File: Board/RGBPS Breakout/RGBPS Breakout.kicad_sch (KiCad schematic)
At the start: 2 parts, among them IC1 APDS-9999, J1 Conn_01x04_Pin

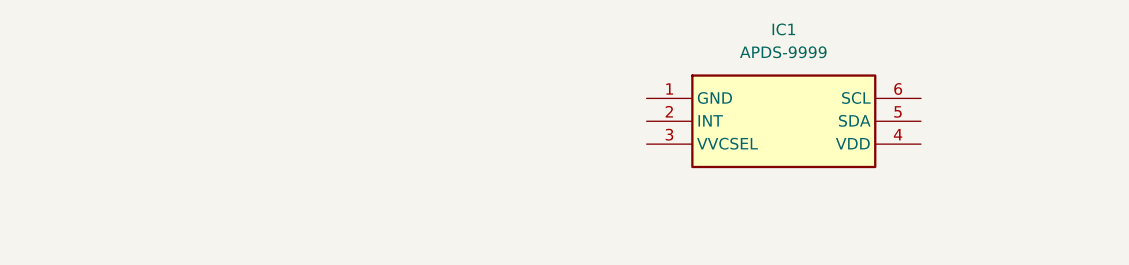
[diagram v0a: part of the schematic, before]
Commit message: indicator/illuminating LED
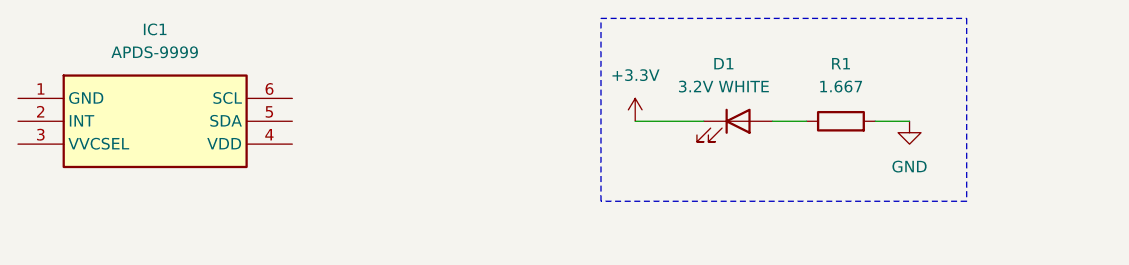
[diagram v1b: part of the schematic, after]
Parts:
- added D1: 3.2V WHITE, symbol Device:LED
- added R1: 1.667, symbol Device:R
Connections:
- net +3.3V: now also D1.1 (K)
- net GND: now also R1.2
- new net: D1.2 (A), R1.1
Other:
- moved on the sheet: IC1

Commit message: partially done with power
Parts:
- added C1, C2: 4u7, symbol Device:C
- added R2: 100, symbol Device:R
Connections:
- net +3.3V: now also IC1.3 (VVCSEL), C2.1, R2.2
- net GND: now also IC1.1 (GND), C1.2, C2.2
- net at IC1.4 (VDD): now also C1.1, R2.1
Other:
- moved on the sheet: D1, IC1, J1, R1

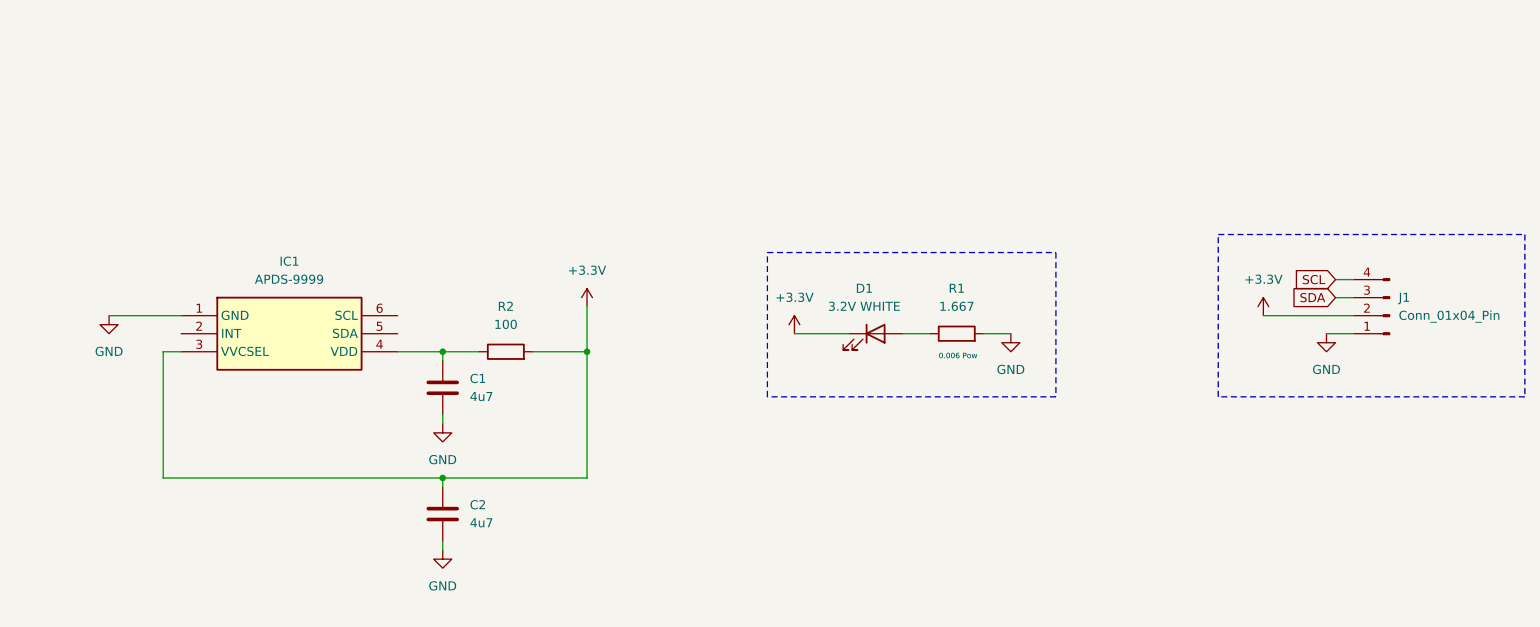
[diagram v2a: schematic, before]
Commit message: i2c wiring + pullup resistors
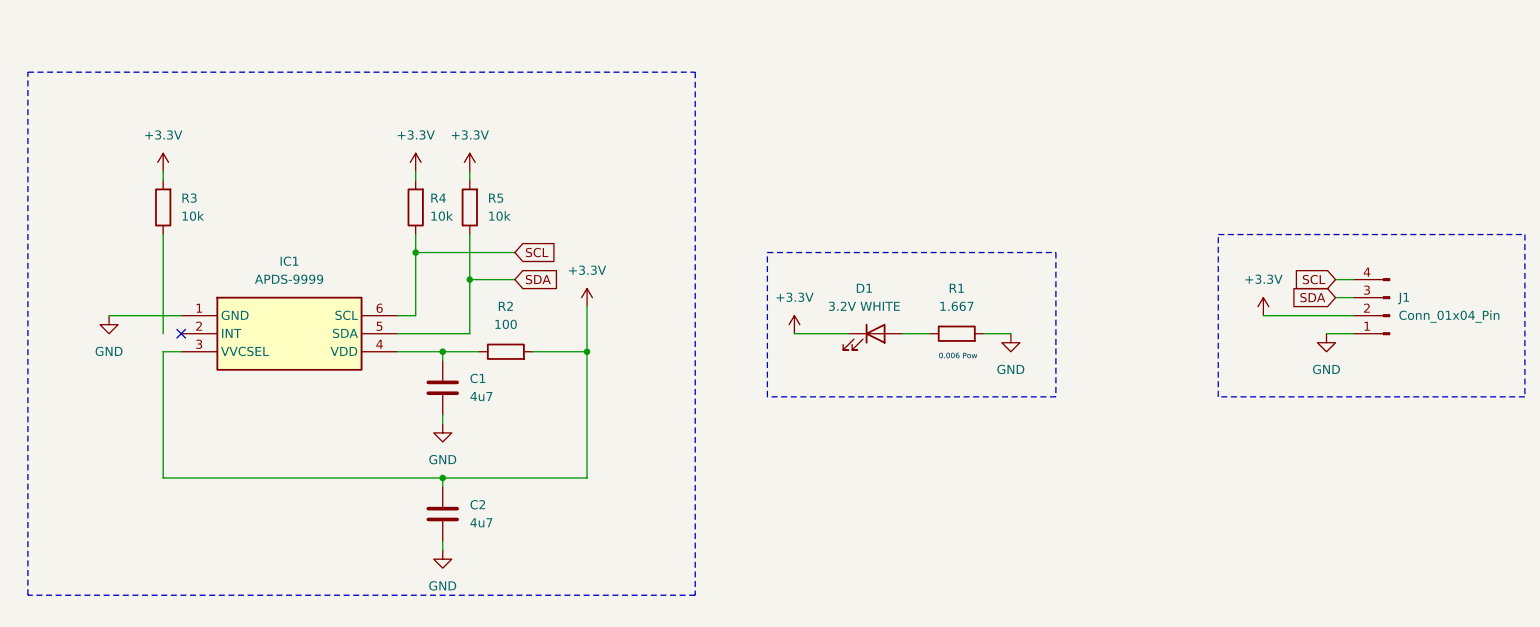
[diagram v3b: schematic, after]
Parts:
- added R3, R4, R5: 10k, symbol Device:R
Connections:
- net +3.3V: now also R3.2, R4.2, R5.2
- net SCL: now also IC1.6 (SCL), R4.1
- net SDA: now also IC1.5 (SDA), R5.1
- no-connect marks 0 -> 1

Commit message: interrupt pin
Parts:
- added J2: Conn_01x01_Pin, symbol Connector:Conn_01x01_Pin
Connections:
- net INT: now reaches IC1.2 (INT)
- net INT: now also R3.1, J2.1 (Pin_1)
- no-connect marks 1 -> 0

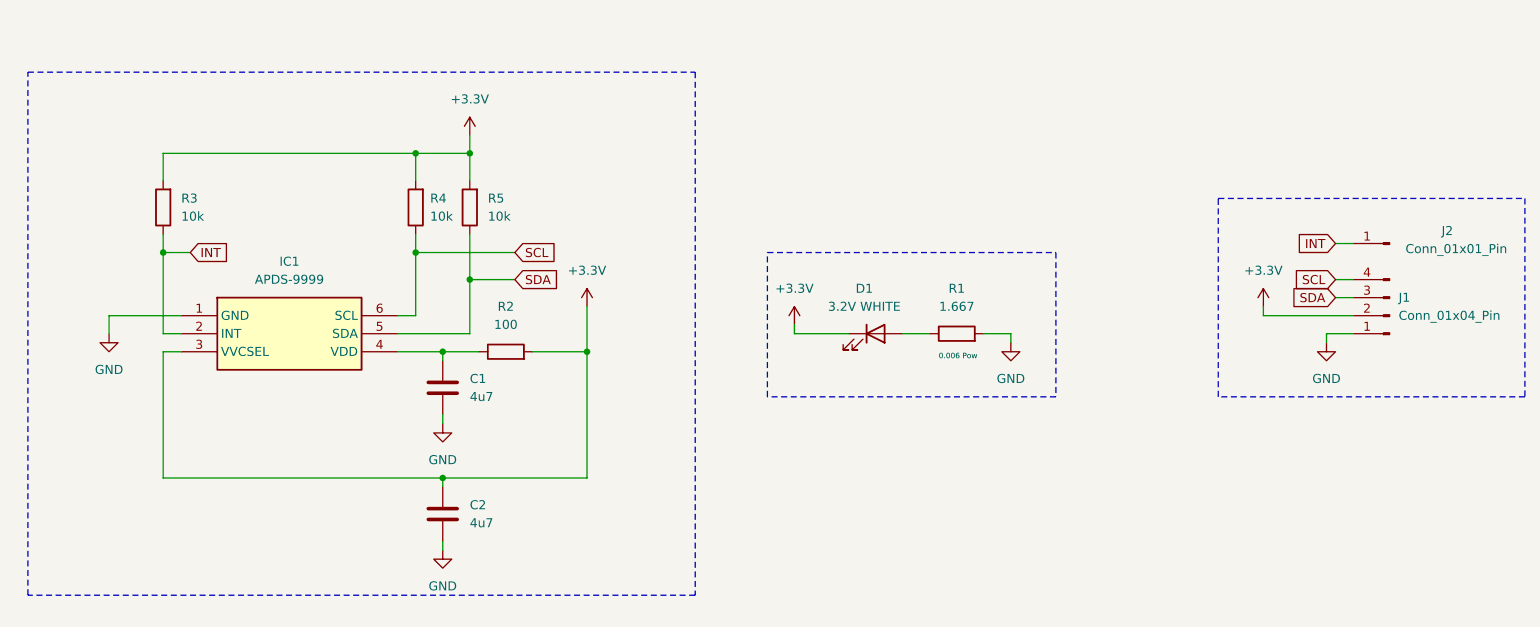
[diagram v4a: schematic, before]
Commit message: footprints except for the sensor
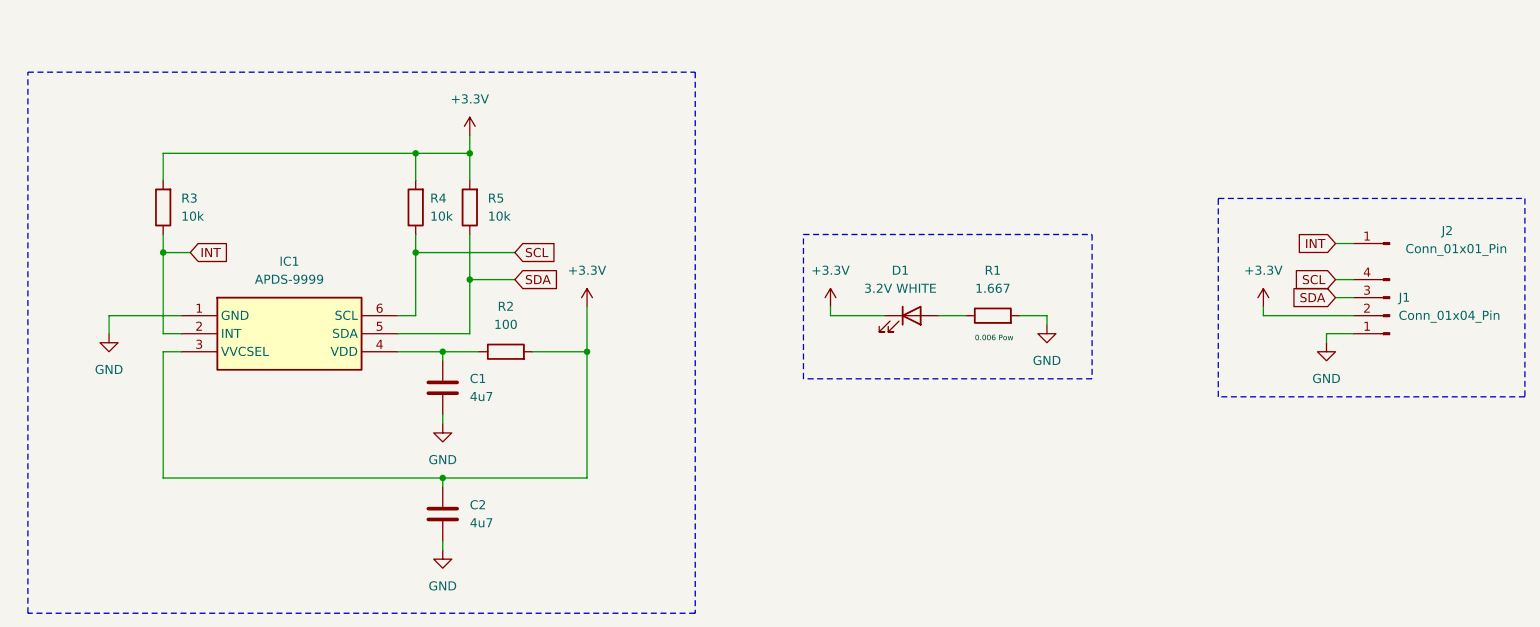
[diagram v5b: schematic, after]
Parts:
- C1, C2: footprint (none) -> Capacitor_SMD:C_0402_1005Metric
- D1: footprint (none) -> LED_SMD:LED_1206_3216Metric
- J1: footprint (none) -> Connector_JST:JST_PH_S4B-PH-K_1x04_P2.00mm_Horizontal
- J2: footprint (none) -> Connector_PinHeader_2.54mm:PinHeader_1x01_P2.54mm_Horizontal
- R1, R2, R3, R4, R5: footprint (none) -> Resistor_SMD:R_0402_1005Metric
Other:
- moved on the sheet: D1, R1
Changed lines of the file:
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@@
 	(wire
 		(pts
-			(xy 189.23 102.87) (xy 189.23 104.14)
+			(xy 194.31 100.33) (xy 194.31 101.6)
 		)
 		(stroke
@@
 	(wire
 		(pts
-			(xy 173.99 102.87) (xy 177.8 102.87)
+			(xy 179.07 100.33) (xy 182.88 100.33)
 		)
 		(stroke
@@
 	(wire
 		(pts
-			(xy 158.75 102.87) (xy 158.75 101.6)
+			(xy 163.83 100.33) (xy 163.83 99.06)
 		)
 		(stroke
@@
 	(wire
 		(pts
-			(xy 189.23 102.87) (xy 185.42 102.87)
+			(xy 194.31 100.33) (xy 190.5 100.33)
 		)
 		(stroke
@@
 	(wire
 		(pts
-			(xy 158.75 102.87) (xy 166.37 102.87)
+			(xy 163.83 100.33) (xy 171.45 100.33)
 		)
 		(stroke
@@
 	)
 	(rectangle
-		(start 154.94 91.44)
-		(end 195.58 111.76)
+		(start 160.02 88.9)
+		(end 200.66 109.22)
 		(stroke
 			(width 0)
@@
 	(rectangle
 		(start 50.8 66.04)
-		(end 144.78 139.7)
+		(end 144.78 142.24)
 		(stroke
 			(width 0)
@@
 	)
 	(label "0.006 Pow"
-		(at 179.07 106.68 0)
+		(at 184.15 104.14 0)
 		(fields_autoplaced yes)
 		(effects
@@
 	(symbol
 		(lib_id "Device:R")
-		(at 181.61 102.87 90)
+		(at 186.69 100.33 90)
 		(unit 1)
 		(exclude_from_sim no)
@@
 		(fields_autoplaced yes)
 		(property "Reference" "R1"
-			(at 181.61 96.52 90)
+			(at 186.69 93.98 90)
 			(effects
 				(font
@@
 		)
 		(property "Value" "1.667"
-			(at 181.61 99.06 90)
-			(effects
-				(font
-					(size 1.27 1.27)
-				)
-			)
-		)
-		(property "Footprint" ""
-			(at 181.61 104.648 90)
+			(at 186.69 96.52 90)
+			(effects
+				(font
+					(size 1.27 1.27)
+				)
+			)
+		)
+		(property "Footprint" "Resistor_SMD:R_0402_1005Metric"
+			(at 186.69 102.108 90)
 			(effects
 				(font
@@
 		)
 		(property "Datasheet" "~"
-			(at 181.61 102.87 0)
+			(at 186.69 100.33 0)
 			(effects
 				(font
@@
 		)
 		(property "Description" "Resistor"
-			(at 181.61 102.87 0)
+			(at 186.69 100.33 0)
 			(effects
 				(font
@@
 	(symbol
 		(lib_id "power:GND")
-		(at 189.23 104.14 0)
+		(at 194.31 101.6 0)
 		(unit 1)
 		(exclude_from_sim no)
@@
 		(fields_autoplaced yes)
 		(property "Reference" "#PWR03"
-			(at 189.23 110.49 0)
+			(at 194.31 107.95 0)
 			(effects
 				(font
@@
 		)
 		(property "Value" "GND"
-			(at 189.23 109.22 0)
+			(at 194.31 106.68 0)
 			(effects
 				(font
@@
 		)
 		(property "Footprint" ""
-			(at 189.23 104.14 0)
+			(at 194.31 101.6 0)
 			(effects
 				(font
@@
 		)
 		(property "Datasheet" ""
-			(at 189.23 104.14 0)
+			(at 194.31 101.6 0)
 			(effects
 				(font
@@
 		)
 		(property "Description" "Power symbol creates a global label with name \"GND\" , ground"
-			(at 189.23 104.14 0)
+			(at 194.31 101.6 0)
 			(effects
 				(font
@@
 	(symbol
 		(lib_id "Device:LED")
-		(at 170.18 102.87 0)
+		(at 175.26 100.33 0)
 		(unit 1)
 		(exclude_from_sim no)
@@
 		(fields_autoplaced yes)
 		(property "Reference" "D1"
-			(at 168.5925 96.52 0)
+			(at 173.6725 93.98 0)
 			(effects
 				(font
@@
 		)
 		(property "Value" "3.2V WHITE"
-			(at 168.5925 99.06 0)
-			(effects
-				(font
-					(size 1.27 1.27)
-				)
-			)
-		)
-		(property "Footprint" ""
-			(at 170.18 102.87 0)
+			(at 173.6725 96.52 0)
+			(effects
+				(font
+					(size 1.27 1.27)
+				)
+			)
+		)
+		(property "Footprint" "LED_SMD:LED_1206_3216Metric"
+			(at 175.26 100.33 0)
 			(effects
 				(font
@@
 		)
 		(property "Datasheet" "~"
-			(at 170.18 102.87 0)
+			(at 175.26 100.33 0)
 			(effects
 				(font
@@
 		)
 		(property "Description" "Light emitting diode"
-			(at 170.18 102.87 0)
+			(at 175.26 100.33 0)
 			(effects
 				(font
@@
 			)
 		)
-		(property "Footprint" ""
+		(property "Footprint" "Resistor_SMD:R_0402_1005Metric"
 			(at 114.808 85.09 90)
 			(effects
@@
 	(symbol
 		(lib_id "power:+3.3V")
-		(at 158.75 101.6 0)
+		(at 163.83 99.06 0)
 		(unit 1)
 		(exclude_from_sim no)
@@
 		(fields_autoplaced yes)
 		(property "Reference" "#PWR04"
-			(at 158.75 105.41 0)
+			(at 163.83 102.87 0)
 			(effects
 				(font
@@
 		)
 		(property "Value" "+3.3V"
-			(at 158.75 96.52 0)
+			(at 163.83 93.98 0)
 			(effects
 				(font
@@
 		)
 		(property "Footprint" ""
-			(at 158.75 101.6 0)
+			(at 163.83 99.06 0)
 			(effects
 				(font
@@
 		)
 		(property "Datasheet" ""
-			(at 158.75 101.6 0)
+			(at 163.83 99.06 0)
 			(effects
 				(font
@@
 		)
 		(property "Description" "Power symbol creates a global label with name \"+3.3V\""
-			(at 158.75 101.6 0)
+			(at 163.83 99.06 0)
 			(effects
 				(font
@@
 			)
 		)
-		(property "Footprint" ""
+		(property "Footprint" "Resistor_SMD:R_0402_1005Metric"
 			(at 118.11 107.188 90)
 			(effects
@@
 			)
 		)
-		(property "Footprint" ""
+		(property "Footprint" "Connector_PinHeader_2.54mm:PinHeader_1x01_P2.54mm_Horizontal"
 			(at 242.57 90.17 0)
 			(effects
@@
 			)
 		)
-		(property "Footprint" ""
+		(property "Footprint" "Capacitor_SMD:C_0402_1005Metric"
 			(at 110.1852 114.3 0)
 			(effects
@@
 			)
 		)
-		(property "Footprint" ""
+		(property "Footprint" "Capacitor_SMD:C_0402_1005Metric"
 			(at 110.1852 132.08 0)
 			(effects
@@
 			)
 		)
-		(property "Footprint" ""
+		(property "Footprint" "Resistor_SMD:R_0402_1005Metric"
 			(at 107.188 85.09 90)
 			(effects
@@
 			)
 		)
-		(property "Footprint" ""
+		(property "Footprint" "Resistor_SMD:R_0402_1005Metric"
 			(at 71.628 85.09 90)
 			(effects
@@
 			)
 		)
-		(property "Footprint" ""
+		(property "Footprint" "Connector_JST:JST_PH_S4B-PH-K_1x04_P2.00mm_Horizontal"
 			(at 242.57 100.33 0)
 			(effects

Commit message: label
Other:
- title: (none) -> RGBPS Breakout
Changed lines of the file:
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@@
 	(generator_version "8.0")
 	(paper "A4")
+	(title_block
+		(title "RGBPS Breakout")
+		(date "2024-07-05")
+		(rev "1")
+	)
 	(junction
 		(at 69.85 91.44)
@@
 			)
 			(justify left bottom)
+		)
+	)
+	(label "Sensor"
+		(at 50.8 64.77 0)
+		(fields_autoplaced yes)
+		(effects
+			(font
+				(size 3.81 3.81)
+				(thickness 0.762)
+				(bold yes)
+			)
+			(justify left bottom)
+		)
+	)
+	(label "Connectors"
+		(at 218.44 83.82 0)
+		(fields_autoplaced yes)
+		(effects
+			(font
+				(size 3.81 3.81)
+				(thickness 0.762)
+				(bold yes)
+			)
+			(justify left bottom)
+		)
+	)
+	(label "LED"
+		(at 158.75 87.63 0)
+		(fields_autoplaced yes)
+		(effects
+			(font
+				(size 3.81 3.81)
+				(thickness 0.762)
+				(bold yes)
+			)
+			(justify left bottom)

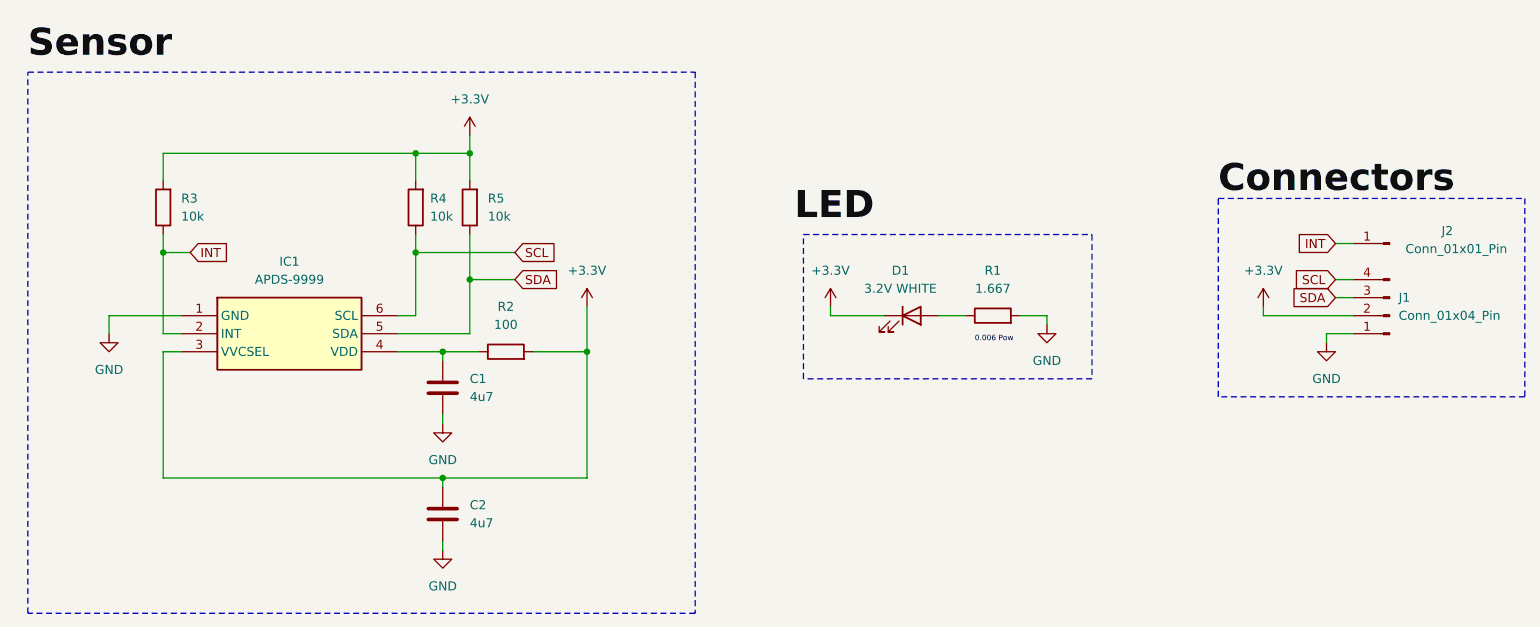
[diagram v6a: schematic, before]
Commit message: pass electrical rules check finally
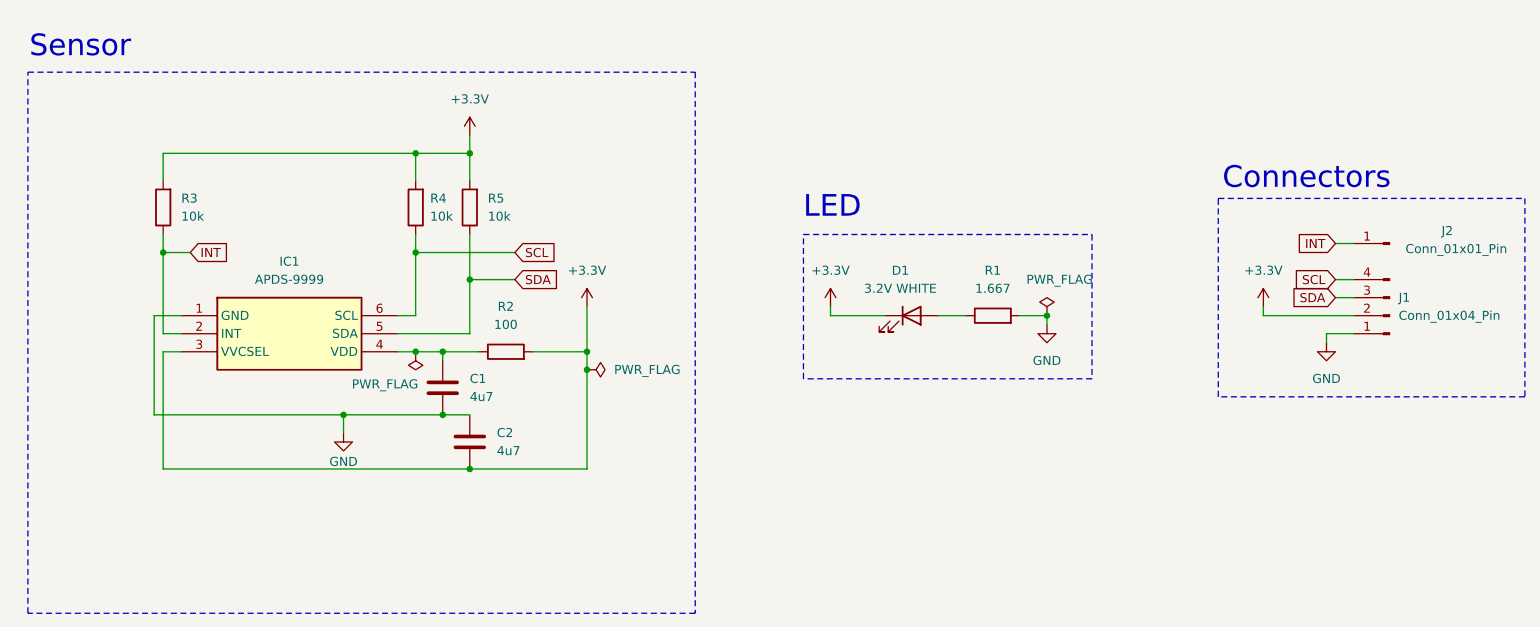
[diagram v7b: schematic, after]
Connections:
- net +3.3V: now also C2.2; no longer C2.1
- net GND: now also C2.1; no longer C2.2
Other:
- note added: "Connectors"
- note added: "LED"
- note added: "Sensor"
- moved on the sheet: C2
